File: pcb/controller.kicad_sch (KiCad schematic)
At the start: 2 parts, among them J1 Teensy 4.1 FEMALE 1x24, J2 Teensy 4.1 FEMALE 1x24

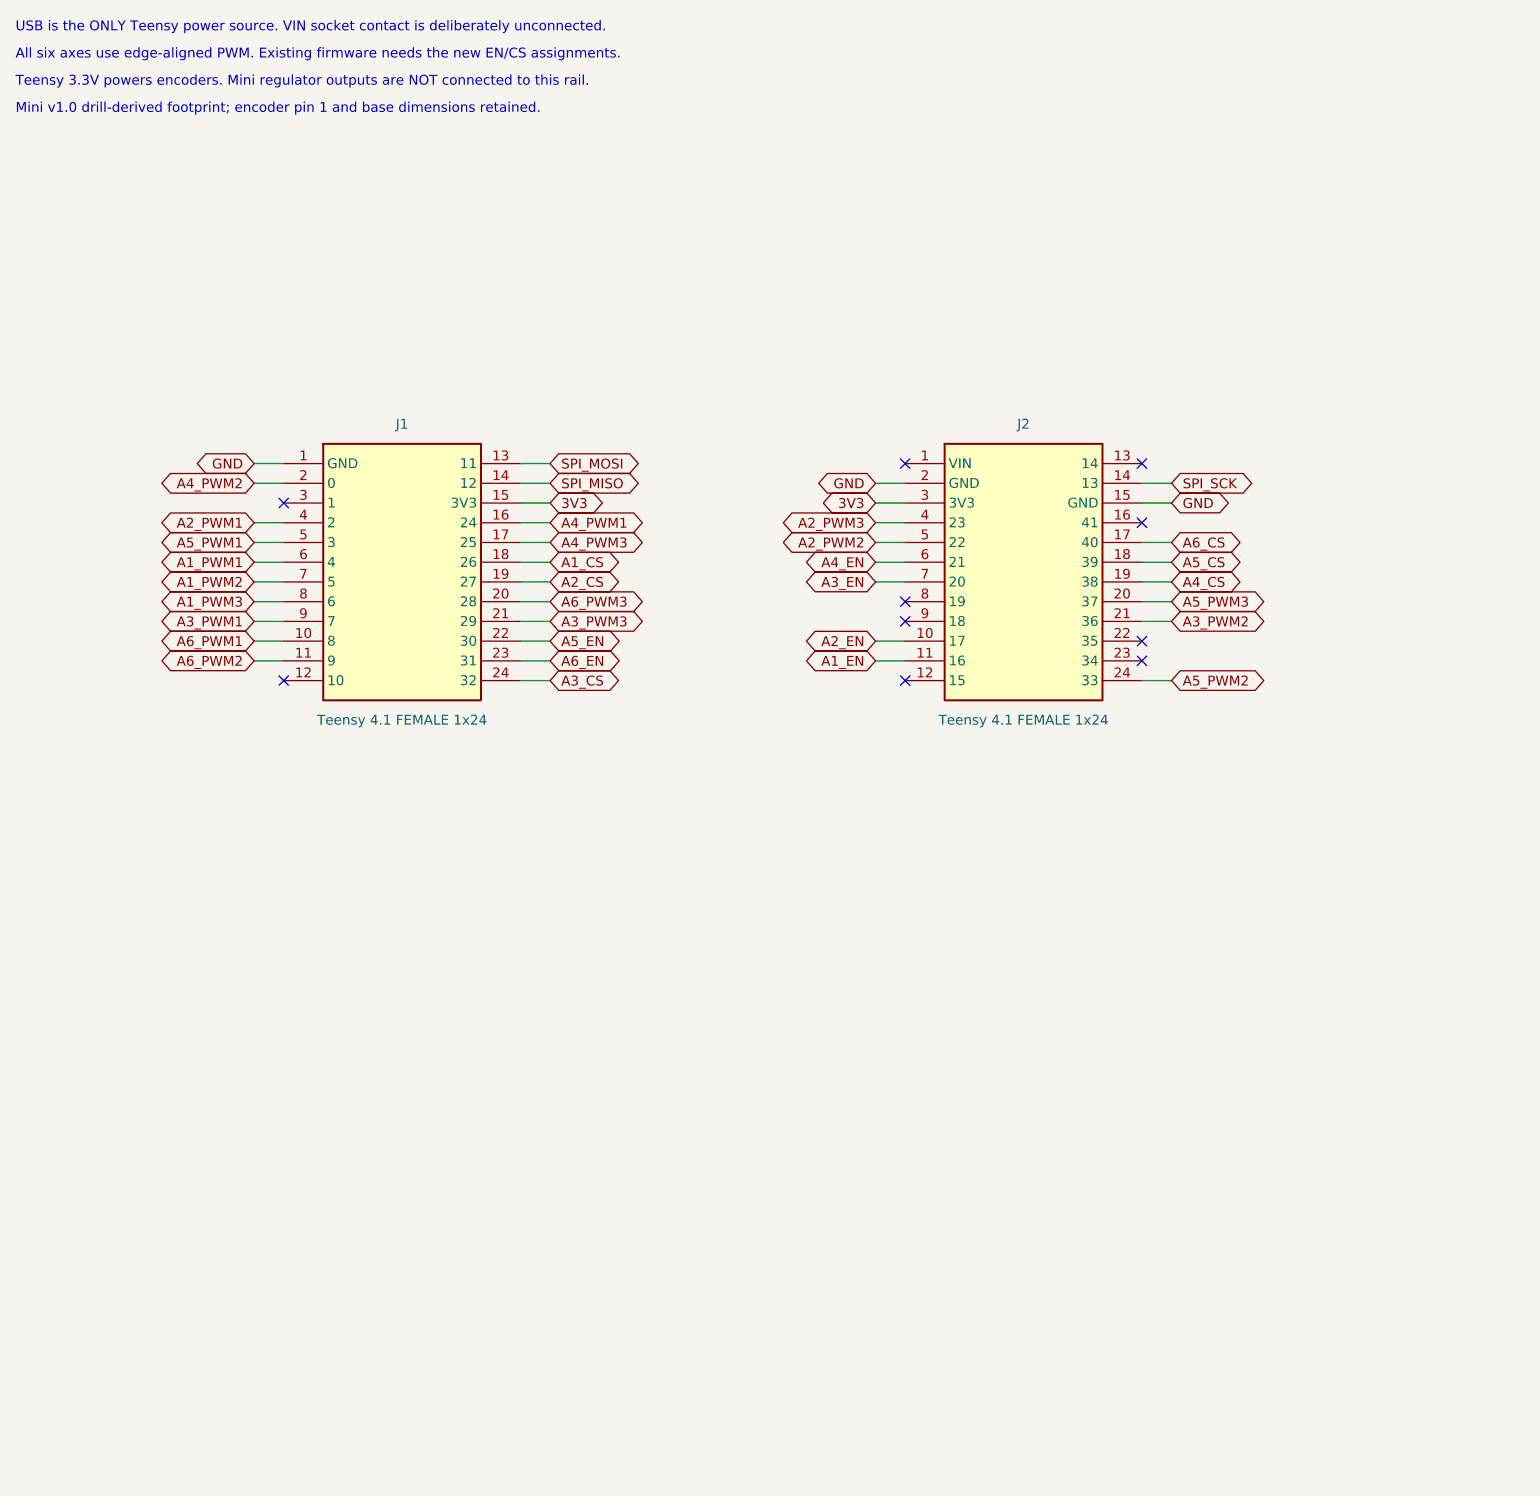
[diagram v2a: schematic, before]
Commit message: feat: relayout carrier with edge connectors and hardware kill
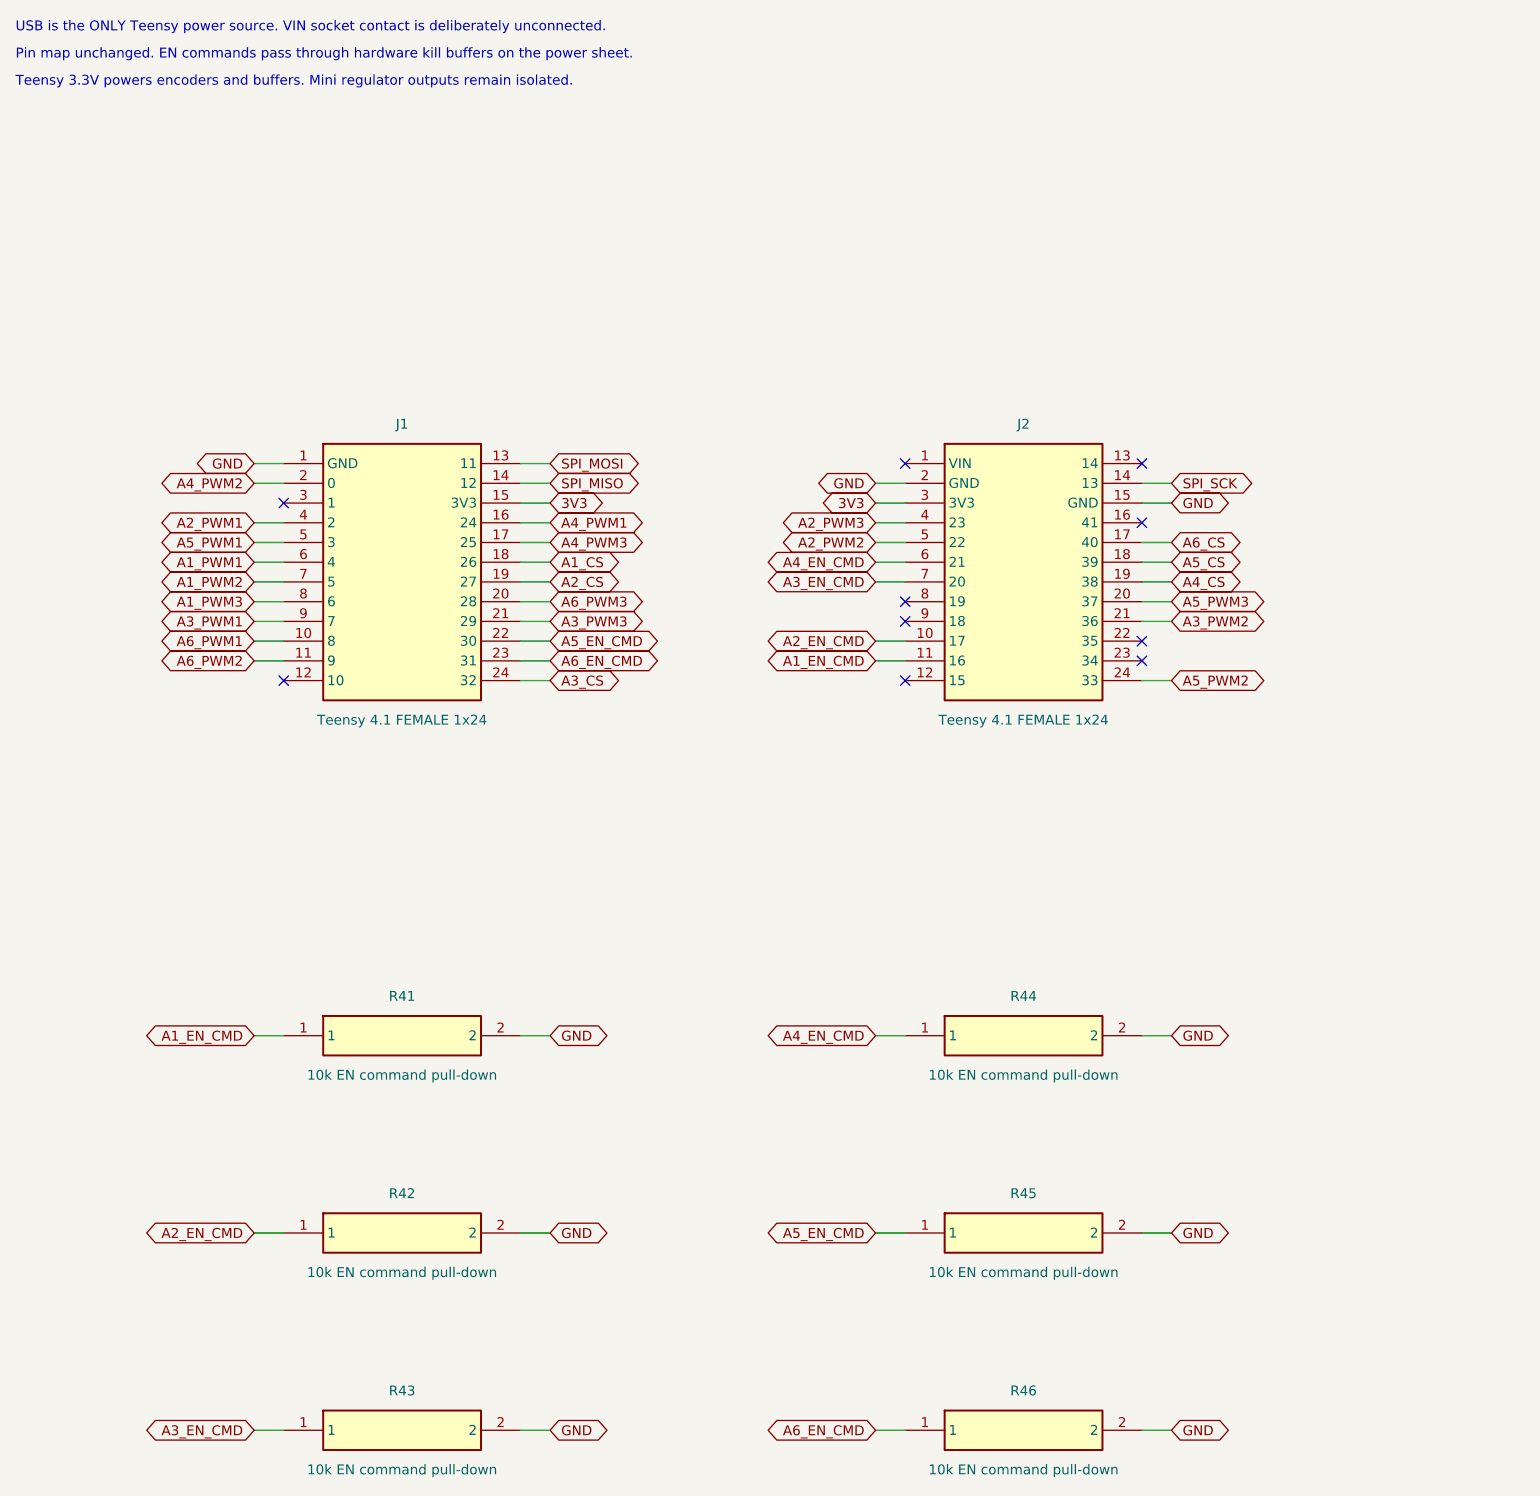
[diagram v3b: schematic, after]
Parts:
- added R41: 10k EN command pull-down, TrueSkate:Edge_R_Axial_DIN0207_L6.3mm_D2.5mm_P7.62mm_Horizontal, symbol TrueSkate:R41
- added R42: 10k EN command pull-down, TrueSkate:Edge_R_Axial_DIN0207_L6.3mm_D2.5mm_P7.62mm_Horizontal, symbol TrueSkate:R42
- added R43: 10k EN command pull-down, TrueSkate:Edge_R_Axial_DIN0207_L6.3mm_D2.5mm_P7.62mm_Horizontal, symbol TrueSkate:R43
- added R44: 10k EN command pull-down, TrueSkate:Edge_R_Axial_DIN0207_L6.3mm_D2.5mm_P7.62mm_Horizontal, symbol TrueSkate:R44
- added R45: 10k EN command pull-down, TrueSkate:Edge_R_Axial_DIN0207_L6.3mm_D2.5mm_P7.62mm_Horizontal, symbol TrueSkate:R45
- added R46: 10k EN command pull-down, TrueSkate:Edge_R_Axial_DIN0207_L6.3mm_D2.5mm_P7.62mm_Horizontal, symbol TrueSkate:R46
- J1, J2: footprint Connector_PinSocket_2.54mm:PinSocket_1x24_P2.54mm_Vertical -> TrueSkate:Edge_PinSocket_1x24_P2.54mm_Vertical
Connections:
- net GND: now also R41.2, R42.2, R43.2, R44.2, R45.2, R46.2
- net A1_EN renamed A1_EN_CMD
- net A1_EN_CMD: now also R41.1
- net A2_EN renamed A2_EN_CMD
- net A2_EN_CMD: now also R42.1
- net A3_EN renamed A3_EN_CMD
- net A3_EN_CMD: now also R43.1
- net A4_EN renamed A4_EN_CMD
- net A4_EN_CMD: now also R44.1
- net A5_EN renamed A5_EN_CMD
- net A5_EN_CMD: now also R45.1
- net A6_EN renamed A6_EN_CMD
- net A6_EN_CMD: now also R46.1
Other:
- note added: "Pin map unchanged. EN commands pass through hardware kill buffers on the power sheet."
- note added: "Teensy 3.3V powers encoders and buffers. Mini regulator outputs remain isolated."
- note removed: "All six axes use edge-aligned PWM. Existing firmware needs the new EN/CS assignments."
- note removed: "Mini v1.0 drill-derived footprint; encoder pin 1 and base dimensions retained."
- note removed: "Teensy 3.3V powers encoders. Mini regulator outputs are NOT connected to this rail."
